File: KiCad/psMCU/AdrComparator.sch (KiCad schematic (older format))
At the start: 8 parts, among them U366 74HC85, U367 74HC85, U368 74LVC1G08, U369 74LVC1G08

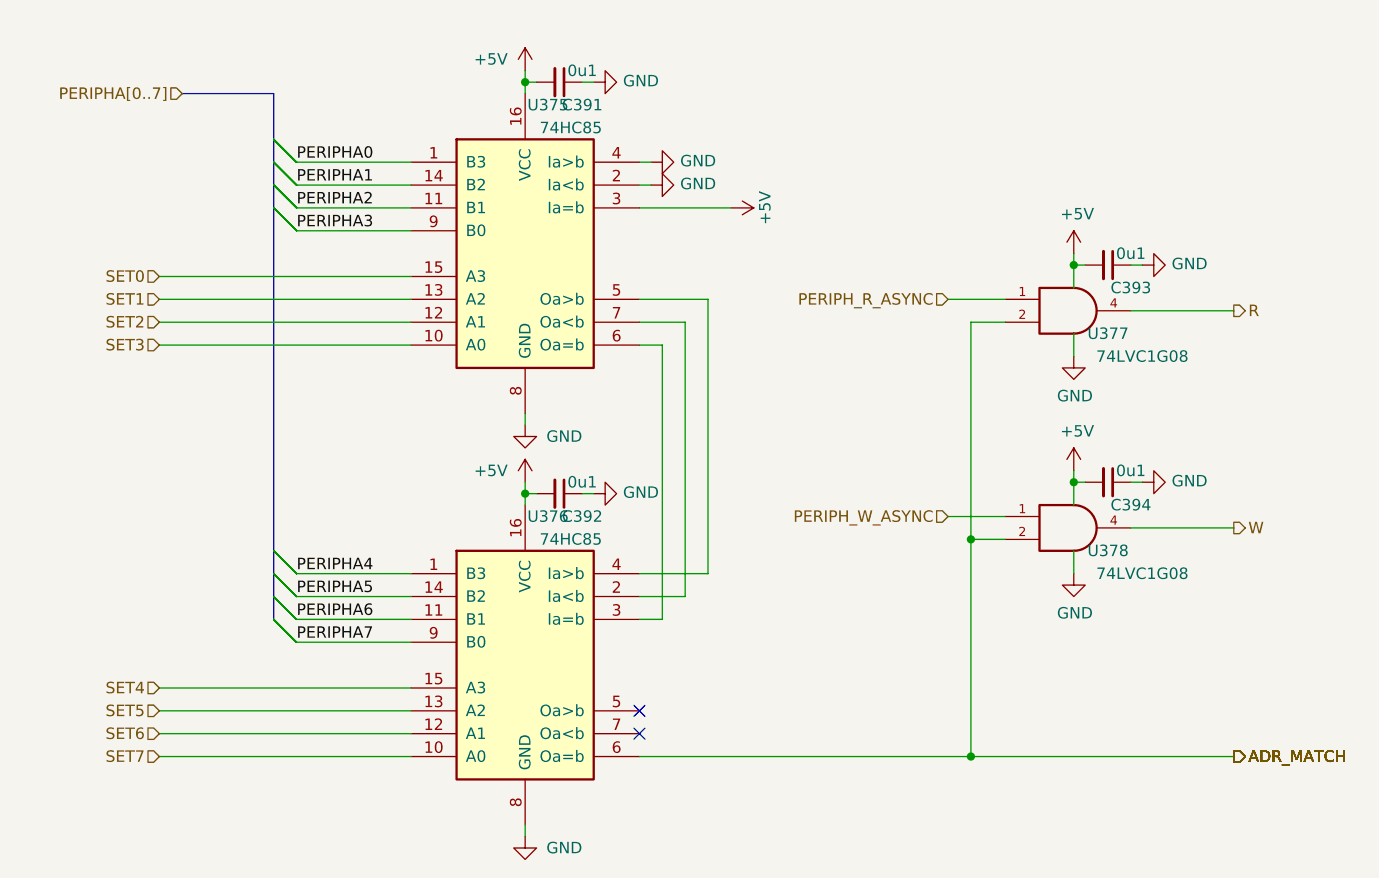
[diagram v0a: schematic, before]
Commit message: Cleanup, ready for specific component values.
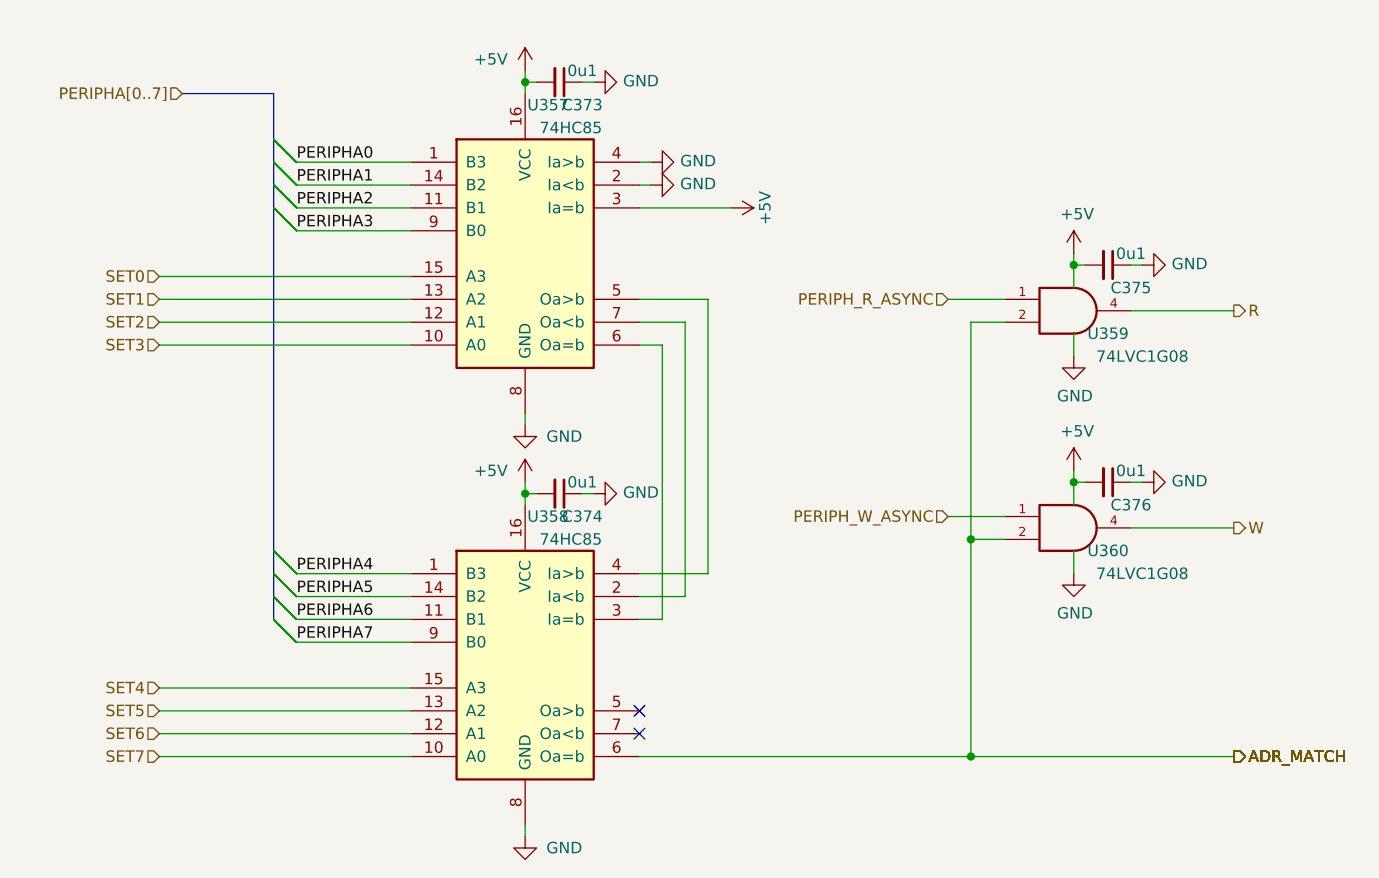
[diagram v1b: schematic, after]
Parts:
- U366, U367: footprint Package_SO:SOIC-16W_5.3x10.2mm_P1.27mm -> Package_SO:SOIC-16_3.9x9.9mm_P1.27mm
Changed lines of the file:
@@
 $Descr A4 11693 8268
 encoding utf-8
-Sheet 111 113
+Sheet 106 110
 Title "psMCU"
 Date ""
@@
 AR Path="/5FD65308/60297285/60250BD0" Ref="#PWR01569"  Part="1"
 AR Path="/5FD65262/605B62FF/60250BD0" Ref="#PWR01647"  Part="1"
-F 0 "#PWR01647" H 4450 1400 50  0001 C CNN
+F 0 "#PWR01569" H 4450 1400 50  0001 C CNN
 F 1 "+5V" H 4300 1600 50  0000 C CNN
 F 2 "" H 4450 1550 50  0001 C CNN
@@
 AR Path="/5FD65308/60297285/60250BD8" Ref="#PWR01573"  Part="1"
 AR Path="/5FD65262/605B62FF/60250BD8" Ref="#PWR01651"  Part="1"
-F 0 "#PWR01651" H 4750 1350 50  0001 C CNN
+F 0 "#PWR01573" H 4750 1350 50  0001 C CNN
 F 1 "GND" V 4755 1472 50  0000 R CNN
 F 2 "" H 4750 1600 50  0001 C CNN
@@
 AR Path="/5FD65308/60297285/60250BE7" Ref="#PWR01570"  Part="1"
 AR Path="/5FD65262/605B62FF/60250BE7" Ref="#PWR01648"  Part="1"
-F 0 "#PWR01648" H 4450 2850 50  0001 C CNN
+F 0 "#PWR01570" H 4450 2850 50  0001 C CNN
 F 1 "GND" H 4700 3050 50  0000 R CNN
 F 2 "" H 4450 3100 50  0001 C CNN
@@
 AR Path="/5FD65308/60297285/605B829D" Ref="#PWR01571"  Part="1"
 AR Path="/5FD65262/605B62FF/605B829D" Ref="#PWR01649"  Part="1"
-F 0 "#PWR01649" H 4450 3200 50  0001 C CNN
+F 0 "#PWR01571" H 4450 3200 50  0001 C CNN
 F 1 "+5V" H 4300 3400 50  0000 C CNN
 F 2 "" H 4450 3350 50  0001 C CNN
@@
 AR Path="/5FD65308/60297285/605B829E" Ref="#PWR01574"  Part="1"
 AR Path="/5FD65262/605B62FF/605B829E" Ref="#PWR01652"  Part="1"
-F 0 "#PWR01652" H 4750 3150 50  0001 C CNN
+F 0 "#PWR01574" H 4750 3150 50  0001 C CNN
 F 1 "GND" V 4755 3272 50  0000 R CNN
 F 2 "" H 4750 3400 50  0001 C CNN
@@
 AR Path="/5FD65308/60297285/60250C0B" Ref="#PWR01572"  Part="1"
 AR Path="/5FD65262/605B62FF/60250C0B" Ref="#PWR01650"  Part="1"
-F 0 "#PWR01650" H 4450 4650 50  0001 C CNN
+F 0 "#PWR01572" H 4450 4650 50  0001 C CNN
 F 1 "GND" H 4700 4850 50  0000 R CNN
 F 2 "" H 4450 4900 50  0001 C CNN
@@
 AR Path="/5FD65308/60297285/605B82A1" Ref="#PWR01575"  Part="1"
 AR Path="/5FD65262/605B62FF/605B82A1" Ref="#PWR01653"  Part="1"
-F 0 "#PWR01653" H 5000 1700 50  0001 C CNN
+F 0 "#PWR01575" H 5000 1700 50  0001 C CNN
 F 1 "GND" V 5005 1822 50  0000 R CNN
 F 2 "" H 5000 1950 50  0001 C CNN
@@
 AR Path="/5FD65308/60297285/605A18AB" Ref="#PWR01583"  Part="1"
 AR Path="/5FD65262/605B62FF/605A18AB" Ref="#PWR01661"  Part="1"
-F 0 "#PWR01661" H 7150 3100 50  0001 C CNN
+F 0 "#PWR01583" H 7150 3100 50  0001 C CNN
 F 1 "GND" V 7155 3222 50  0000 R CNN
 F 2 "" H 7150 3350 50  0001 C CNN
@@
 AR Path="/5FD65308/60297285/605B82CA" Ref="#PWR01580"  Part="1"
 AR Path="/5FD65262/605B62FF/605B82CA" Ref="#PWR01658"  Part="1"
-F 0 "#PWR01658" H 6850 3150 50  0001 C CNN
+F 0 "#PWR01580" H 6850 3150 50  0001 C CNN
 F 1 "+5V" H 6865 3473 50  0000 C CNN
 F 2 "" H 6850 3300 50  0001 C CNN
@@
 AR Path="/5FD65308/60297285/605A18B0" Ref="#PWR01582"  Part="1"
 AR Path="/5FD65262/605B62FF/605A18B0" Ref="#PWR01660"  Part="1"
-F 0 "#PWR01660" H 7150 2150 50  0001 C CNN
+F 0 "#PWR01582" H 7150 2150 50  0001 C CNN
 F 1 "GND" V 7155 2272 50  0000 R CNN
 F 2 "" H 7150 2400 50  0001 C CNN
@@
 AR Path="/5FD65308/60297285/605A18B2" Ref="#PWR01578"  Part="1"
 AR Path="/5FD65262/605B62FF/605A18B2" Ref="#PWR01656"  Part="1"
-F 0 "#PWR01656" H 6850 2200 50  0001 C CNN
+F 0 "#PWR01578" H 6850 2200 50  0001 C CNN
 F 1 "+5V" H 6865 2523 50  0000 C CNN
 F 2 "" H 6850 2350 50  0001 C CNN
@@
 AR Path="/5FD65308/60297285/605A18B3" Ref="#PWR01579"  Part="1"
 AR Path="/5FD65262/605B62FF/605A18B3" Ref="#PWR01657"  Part="1"
-F 0 "#PWR01657" H 6850 2550 50  0001 C CNN
+F 0 "#PWR01579" H 6850 2550 50  0001 C CNN
 F 1 "GND" H 6855 2627 50  0000 C CNN
 F 2 "" H 6850 2800 50  0001 C CNN
@@
 AR Path="/5FD65308/60297285/605A189C" Ref="U358"  Part="1"
 AR Path="/5FD65262/605B62FF/605A189C" Ref="U376"  Part="1"
-F 0 "U376" H 4550 4800 50  0000 C CNN
+F 0 "U358" H 4550 4800 50  0000 C CNN
 F 1 "74HC85" H 4650 4700 50  0000 C CNN
-F 2 "Package_SO:SOIC-16W_5.3x10.2mm_P1.27mm" H 4450 4150 50  0001 C CNN
+F 2 "Package_SO:SOIC-16_3.9x9.9mm_P1.27mm" H 4450 4150 50  0001 C CNN
 F 3 "http://www.ti.com/lit/gpn/sn74LS85" H 4450 4150 50  0001 C CNN
 	1    4450 4150
@@
 AR Path="/5FD65308/60297285/605A18B4" Ref="U359"  Part="1"
 AR Path="/5FD65262/605B62FF/605A18B4" Ref="U377"  Part="1"
-F 0 "U377" H 7000 2500 50  0000 C CNN
+F 0 "U359" H 7000 2500 50  0000 C CNN
 F 1 "74LVC1G08" H 7150 2400 50  0000 C CNN
 F 2 "Package_TO_SOT_SMD:SOT-353_SC-70-5" H 6850 2600 50  0001 C CNN
@@
 AR Path="/5FD65308/60297285/6065613A" Ref="C375"  Part="1"
 AR Path="/5FD65262/605B62FF/6065613A" Ref="C393"  Part="1"
-F 0 "C393" V 7100 2500 50  0000 C CNN
+F 0 "C375" V 7100 2500 50  0000 C CNN
 F 1 "0u1" V 6950 2500 50  0000 C CNN
 F 2 "NoRef_Footprints:C_0603_1608Metric_NoRef" H 7000 2400 50  0001 C CNN
@@
 AR Path="/5FD65308/60297285/605A18A4" Ref="U357"  Part="1"
 AR Path="/5FD65262/605B62FF/605A18A4" Ref="U375"  Part="1"
-F 0 "U375" H 4550 3000 50  0000 C CNN
+F 0 "U357" H 4550 3000 50  0000 C CNN
 F 1 "74HC85" H 4650 2900 50  0000 C CNN
-F 2 "Package_SO:SOIC-16W_5.3x10.2mm_P1.27mm" H 4450 2350 50  0001 C CNN
+F 2 "Package_SO:SOIC-16_3.9x9.9mm_P1.27mm" H 4450 2350 50  0001 C CNN
 F 3 "http://www.ti.com/lit/gpn/sn74LS85" H 4450 2350 50  0001 C CNN
 	1    4450 2350
@@
 AR Path="/5FD65308/60297285/605B829F" Ref="C374"  Part="1"
 AR Path="/5FD65262/605B62FF/605B829F" Ref="C392"  Part="1"
-F 0 "C392" V 4700 3500 50  0000 C CNN
+F 0 "C374" V 4700 3500 50  0000 C CNN
 F 1 "0u1" V 4550 3500 50  0000 C CNN
 F 2 "NoRef_Footprints:C_0603_1608Metric_NoRef" H 4600 3400 50  0001 C CNN
@@
 AR Path="/5FD65308/60297285/605A18A2" Ref="#PWR01576"  Part="1"
 AR Path="/5FD65262/605B62FF/605A18A2" Ref="#PWR01654"  Part="1"
-F 0 "#PWR01654" H 5000 1800 50  0001 C CNN
+F 0 "#PWR01576" H 5000 1800 50  0001 C CNN
 F 1 "GND" V 5005 1922 50  0000 R CNN
 F 2 "" H 5000 2050 50  0001 C CNN
@@
 AR Path="/5FD65308/60297285/605A18A3" Ref="#PWR01577"  Part="1"
 AR Path="/5FD65262/605B62FF/605A18A3" Ref="#PWR01655"  Part="1"
-F 0 "#PWR01655" H 5350 2000 50  0001 C CNN
+F 0 "#PWR01577" H 5350 2000 50  0001 C CNN
 F 1 "+5V" H 5350 2300 50  0000 C CNN
 F 2 "" H 5350 2150 50  0001 C CNN
@@
 AR Path="/5FD65308/60297285/605A189A" Ref="C373"  Part="1"
 AR Path="/5FD65262/605B62FF/605A189A" Ref="C391"  Part="1"
-F 0 "C391" V 4700 1700 50  0000 C CNN
+F 0 "C373" V 4700 1700 50  0000 C CNN
 F 1 "0u1" V 4550 1700 50  0000 C CNN
 F 2 "NoRef_Footprints:C_0603_1608Metric_NoRef" H 4600 1600 50  0001 C CNN
@@
 AR Path="/5FD65308/60297285/605A18AF" Ref="U360"  Part="1"
 AR Path="/5FD65262/605B62FF/605A18AF" Ref="U378"  Part="1"
-F 0 "U378" H 7000 3450 50  0000 C CNN
+F 0 "U360" H 7000 3450 50  0000 C CNN
 F 1 "74LVC1G08" H 7150 3350 50  0000 C CNN
 F 2 "Package_TO_SOT_SMD:SOT-353_SC-70-5" H 6850 3550 50  0001 C CNN
@@
 AR Path="/5FD65308/60297285/605B82CB" Ref="#PWR01581"  Part="1"
 AR Path="/5FD65262/605B62FF/605B82CB" Ref="#PWR01659"  Part="1"
-F 0 "#PWR01659" H 6850 3500 50  0001 C CNN
+F 0 "#PWR01581" H 6850 3500 50  0001 C CNN
 F 1 "GND" H 6855 3577 50  0000 C CNN
 F 2 "" H 6850 3750 50  0001 C CNN
@@
 AR Path="/5FD65308/60297285/6065453A" Ref="C376"  Part="1"
 AR Path="/5FD65262/605B62FF/6065453A" Ref="C394"  Part="1"
-F 0 "C394" V 7100 3450 50  0000 C CNN
+F 0 "C376" V 7100 3450 50  0000 C CNN
 F 1 "0u1" V 6950 3450 50  0000 C CNN
 F 2 "NoRef_Footprints:C_0603_1608Metric_NoRef" H 7000 3350 50  0001 C CNN

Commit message: Updated values and footprints.
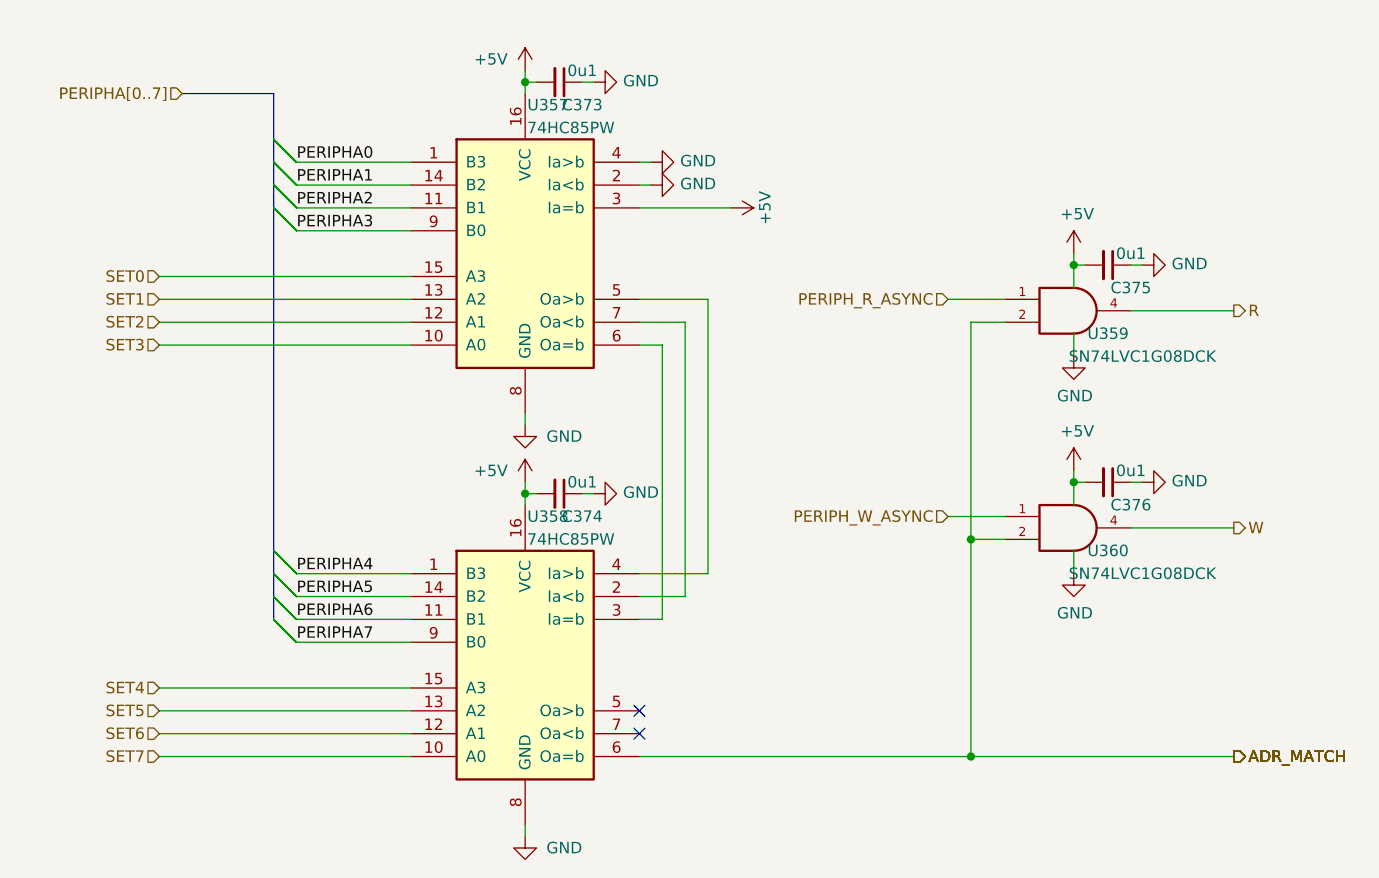
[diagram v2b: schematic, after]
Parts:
- U366, U367: value 74HC85 -> 74HC85PW; footprint Package_SO:SOIC-16_3.9x9.9mm_P1.27mm -> Package_SO:TSSOP-16_4.4x5mm_P0.65mm
- U368, U369: value 74LVC1G08 -> SN74LVC1G08DCK
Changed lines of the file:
@@
 AR Path="/5FD65308/60297285/60250BD0" Ref="#PWR01569"  Part="1"
 AR Path="/5FD65262/605B62FF/60250BD0" Ref="#PWR01647"  Part="1"
-F 0 "#PWR01569" H 4450 1400 50  0001 C CNN
+F 0 "#PWR01647" H 4450 1400 50  0001 C CNN
 F 1 "+5V" H 4300 1600 50  0000 C CNN
 F 2 "" H 4450 1550 50  0001 C CNN
@@
 AR Path="/5FD65308/60297285/60250BD8" Ref="#PWR01573"  Part="1"
 AR Path="/5FD65262/605B62FF/60250BD8" Ref="#PWR01651"  Part="1"
-F 0 "#PWR01573" H 4750 1350 50  0001 C CNN
+F 0 "#PWR01651" H 4750 1350 50  0001 C CNN
 F 1 "GND" V 4755 1472 50  0000 R CNN
 F 2 "" H 4750 1600 50  0001 C CNN
@@
 AR Path="/5FD65308/60297285/60250BE7" Ref="#PWR01570"  Part="1"
 AR Path="/5FD65262/605B62FF/60250BE7" Ref="#PWR01648"  Part="1"
-F 0 "#PWR01570" H 4450 2850 50  0001 C CNN
+F 0 "#PWR01648" H 4450 2850 50  0001 C CNN
 F 1 "GND" H 4700 3050 50  0000 R CNN
 F 2 "" H 4450 3100 50  0001 C CNN
@@
 AR Path="/5FD65308/60297285/605B829D" Ref="#PWR01571"  Part="1"
 AR Path="/5FD65262/605B62FF/605B829D" Ref="#PWR01649"  Part="1"
-F 0 "#PWR01571" H 4450 3200 50  0001 C CNN
+F 0 "#PWR01649" H 4450 3200 50  0001 C CNN
 F 1 "+5V" H 4300 3400 50  0000 C CNN
 F 2 "" H 4450 3350 50  0001 C CNN
@@
 AR Path="/5FD65308/60297285/605B829E" Ref="#PWR01574"  Part="1"
 AR Path="/5FD65262/605B62FF/605B829E" Ref="#PWR01652"  Part="1"
-F 0 "#PWR01574" H 4750 3150 50  0001 C CNN
+F 0 "#PWR01652" H 4750 3150 50  0001 C CNN
 F 1 "GND" V 4755 3272 50  0000 R CNN
 F 2 "" H 4750 3400 50  0001 C CNN
@@
 AR Path="/5FD65308/60297285/60250C0B" Ref="#PWR01572"  Part="1"
 AR Path="/5FD65262/605B62FF/60250C0B" Ref="#PWR01650"  Part="1"
-F 0 "#PWR01572" H 4450 4650 50  0001 C CNN
+F 0 "#PWR01650" H 4450 4650 50  0001 C CNN
 F 1 "GND" H 4700 4850 50  0000 R CNN
 F 2 "" H 4450 4900 50  0001 C CNN
@@
 AR Path="/5FD65308/60297285/605B82A1" Ref="#PWR01575"  Part="1"
 AR Path="/5FD65262/605B62FF/605B82A1" Ref="#PWR01653"  Part="1"
-F 0 "#PWR01575" H 5000 1700 50  0001 C CNN
+F 0 "#PWR01653" H 5000 1700 50  0001 C CNN
 F 1 "GND" V 5005 1822 50  0000 R CNN
 F 2 "" H 5000 1950 50  0001 C CNN
@@
 AR Path="/5FD65308/60297285/605A18AB" Ref="#PWR01583"  Part="1"
 AR Path="/5FD65262/605B62FF/605A18AB" Ref="#PWR01661"  Part="1"
-F 0 "#PWR01583" H 7150 3100 50  0001 C CNN
+F 0 "#PWR01661" H 7150 3100 50  0001 C CNN
 F 1 "GND" V 7155 3222 50  0000 R CNN
 F 2 "" H 7150 3350 50  0001 C CNN
@@
 AR Path="/5FD65308/60297285/605B82CA" Ref="#PWR01580"  Part="1"
 AR Path="/5FD65262/605B62FF/605B82CA" Ref="#PWR01658"  Part="1"
-F 0 "#PWR01580" H 6850 3150 50  0001 C CNN
+F 0 "#PWR01658" H 6850 3150 50  0001 C CNN
 F 1 "+5V" H 6865 3473 50  0000 C CNN
 F 2 "" H 6850 3300 50  0001 C CNN
@@
 AR Path="/5FD65308/60297285/605A18B0" Ref="#PWR01582"  Part="1"
 AR Path="/5FD65262/605B62FF/605A18B0" Ref="#PWR01660"  Part="1"
-F 0 "#PWR01582" H 7150 2150 50  0001 C CNN
+F 0 "#PWR01660" H 7150 2150 50  0001 C CNN
 F 1 "GND" V 7155 2272 50  0000 R CNN
 F 2 "" H 7150 2400 50  0001 C CNN
@@
 AR Path="/5FD65308/60297285/605A18B2" Ref="#PWR01578"  Part="1"
 AR Path="/5FD65262/605B62FF/605A18B2" Ref="#PWR01656"  Part="1"
-F 0 "#PWR01578" H 6850 2200 50  0001 C CNN
+F 0 "#PWR01656" H 6850 2200 50  0001 C CNN
 F 1 "+5V" H 6865 2523 50  0000 C CNN
 F 2 "" H 6850 2350 50  0001 C CNN
@@
 AR Path="/5FD65308/60297285/605A18B3" Ref="#PWR01579"  Part="1"
 AR Path="/5FD65262/605B62FF/605A18B3" Ref="#PWR01657"  Part="1"
-F 0 "#PWR01579" H 6850 2550 50  0001 C CNN
+F 0 "#PWR01657" H 6850 2550 50  0001 C CNN
 F 1 "GND" H 6855 2627 50  0000 C CNN
 F 2 "" H 6850 2800 50  0001 C CNN
@@
 AR Path="/5FD65262/605B62FF/605A189C" Ref="U376"  Part="1"
 F 0 "U358" H 4550 4800 50  0000 C CNN
-F 1 "74HC85" H 4650 4700 50  0000 C CNN
-F 2 "Package_SO:SOIC-16_3.9x9.9mm_P1.27mm" H 4450 4150 50  0001 C CNN
+F 1 "74HC85PW" H 4650 4700 50  0000 C CNN
+F 2 "Package_SO:TSSOP-16_4.4x5mm_P0.65mm" H 4450 4150 50  0001 C CNN
 F 3 "http://www.ti.com/lit/gpn/sn74LS85" H 4450 4150 50  0001 C CNN
 	1    4450 4150
@@
 AR Path="/5FD65262/605B62FF/605A18B4" Ref="U377"  Part="1"
 F 0 "U359" H 7000 2500 50  0000 C CNN
-F 1 "74LVC1G08" H 7150 2400 50  0000 C CNN
+F 1 "SN74LVC1G08DCK" H 7150 2400 50  0000 C CNN
 F 2 "Package_TO_SOT_SMD:SOT-353_SC-70-5" H 6850 2600 50  0001 C CNN
 F 3 "http://www.ti.com/lit/sg/scyt129e/scyt129e.pdf" H 6850 2600 50  0001 C CNN
@@
 AR Path="/5FD65262/605B62FF/605A18A4" Ref="U375"  Part="1"
 F 0 "U357" H 4550 3000 50  0000 C CNN
-F 1 "74HC85" H 4650 2900 50  0000 C CNN
-F 2 "Package_SO:SOIC-16_3.9x9.9mm_P1.27mm" H 4450 2350 50  0001 C CNN
+F 1 "74HC85PW" H 4650 2900 50  0000 C CNN
+F 2 "Package_SO:TSSOP-16_4.4x5mm_P0.65mm" H 4450 2350 50  0001 C CNN
 F 3 "http://www.ti.com/lit/gpn/sn74LS85" H 4450 2350 50  0001 C CNN
 	1    4450 2350
@@
 AR Path="/5FD65308/60297285/605A18A2" Ref="#PWR01576"  Part="1"
 AR Path="/5FD65262/605B62FF/605A18A2" Ref="#PWR01654"  Part="1"
-F 0 "#PWR01576" H 5000 1800 50  0001 C CNN
+F 0 "#PWR01654" H 5000 1800 50  0001 C CNN
 F 1 "GND" V 5005 1922 50  0000 R CNN
 F 2 "" H 5000 2050 50  0001 C CNN
@@
 AR Path="/5FD65308/60297285/605A18A3" Ref="#PWR01577"  Part="1"
 AR Path="/5FD65262/605B62FF/605A18A3" Ref="#PWR01655"  Part="1"
-F 0 "#PWR01577" H 5350 2000 50  0001 C CNN
+F 0 "#PWR01655" H 5350 2000 50  0001 C CNN
 F 1 "+5V" H 5350 2300 50  0000 C CNN
 F 2 "" H 5350 2150 50  0001 C CNN
@@
 AR Path="/5FD65262/605B62FF/605A18AF" Ref="U378"  Part="1"
 F 0 "U360" H 7000 3450 50  0000 C CNN
-F 1 "74LVC1G08" H 7150 3350 50  0000 C CNN
+F 1 "SN74LVC1G08DCK" H 7150 3350 50  0000 C CNN
 F 2 "Package_TO_SOT_SMD:SOT-353_SC-70-5" H 6850 3550 50  0001 C CNN
 F 3 "http://www.ti.com/lit/sg/scyt129e/scyt129e.pdf" H 6850 3550 50  0001 C CNN
@@
 AR Path="/5FD65308/60297285/605B82CB" Ref="#PWR01581"  Part="1"
 AR Path="/5FD65262/605B62FF/605B82CB" Ref="#PWR01659"  Part="1"
-F 0 "#PWR01581" H 6850 3500 50  0001 C CNN
+F 0 "#PWR01659" H 6850 3500 50  0001 C CNN
 F 1 "GND" H 6855 3577 50  0000 C CNN
 F 2 "" H 6850 3750 50  0001 C CNN
